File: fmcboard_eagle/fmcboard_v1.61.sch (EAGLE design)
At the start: 202 parts, among them IC1 OPA695IDR, IC10 LM358, IC11 7805TV, IC12 SN74AUC2G66DCTR, IC13 SN74AUC2G66DCTR, IC14 SN74AUC2G66DCTR, IC15 SN74AUC2G66DCTR, IC16 DAC7578SPWR, IC17 SN74AUC2G66DCTR, IC18 SN74AUC2G66DCTR, IC19 SN74AUC2G66DCTR, IC2 DAC7578SPWR, IC20 SN74AUC2G66DCTR, IC21 74AUP2GU04GW, IC22 74AUP2GU04GW, IC23 74AUP2GU04GW, IC24 74AUP2GU04GW, IC26 AMS1117-1.8, IC27 OPA699ID, IC3 LTC6229IMS8E#TRPBF, IC4 OPA695IDR, IC5 LTC6229IMS8E#TRPBF, IC6 OPA695IDR, IC7 OPA699ID, IC8 LM358, IC9 LM358, J1 8pin, J12 4p-2.54, J2 ASP-134604-01, J3 4p-2.54, J4 4p-2.54, J5 8pin, J6 4p-2.54, J7 4p-2.54, J8 4p-2.54, J9 8pin, U1 TXS0108EPWR, U2 STMICROELECTRONICS_L7905ACVST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

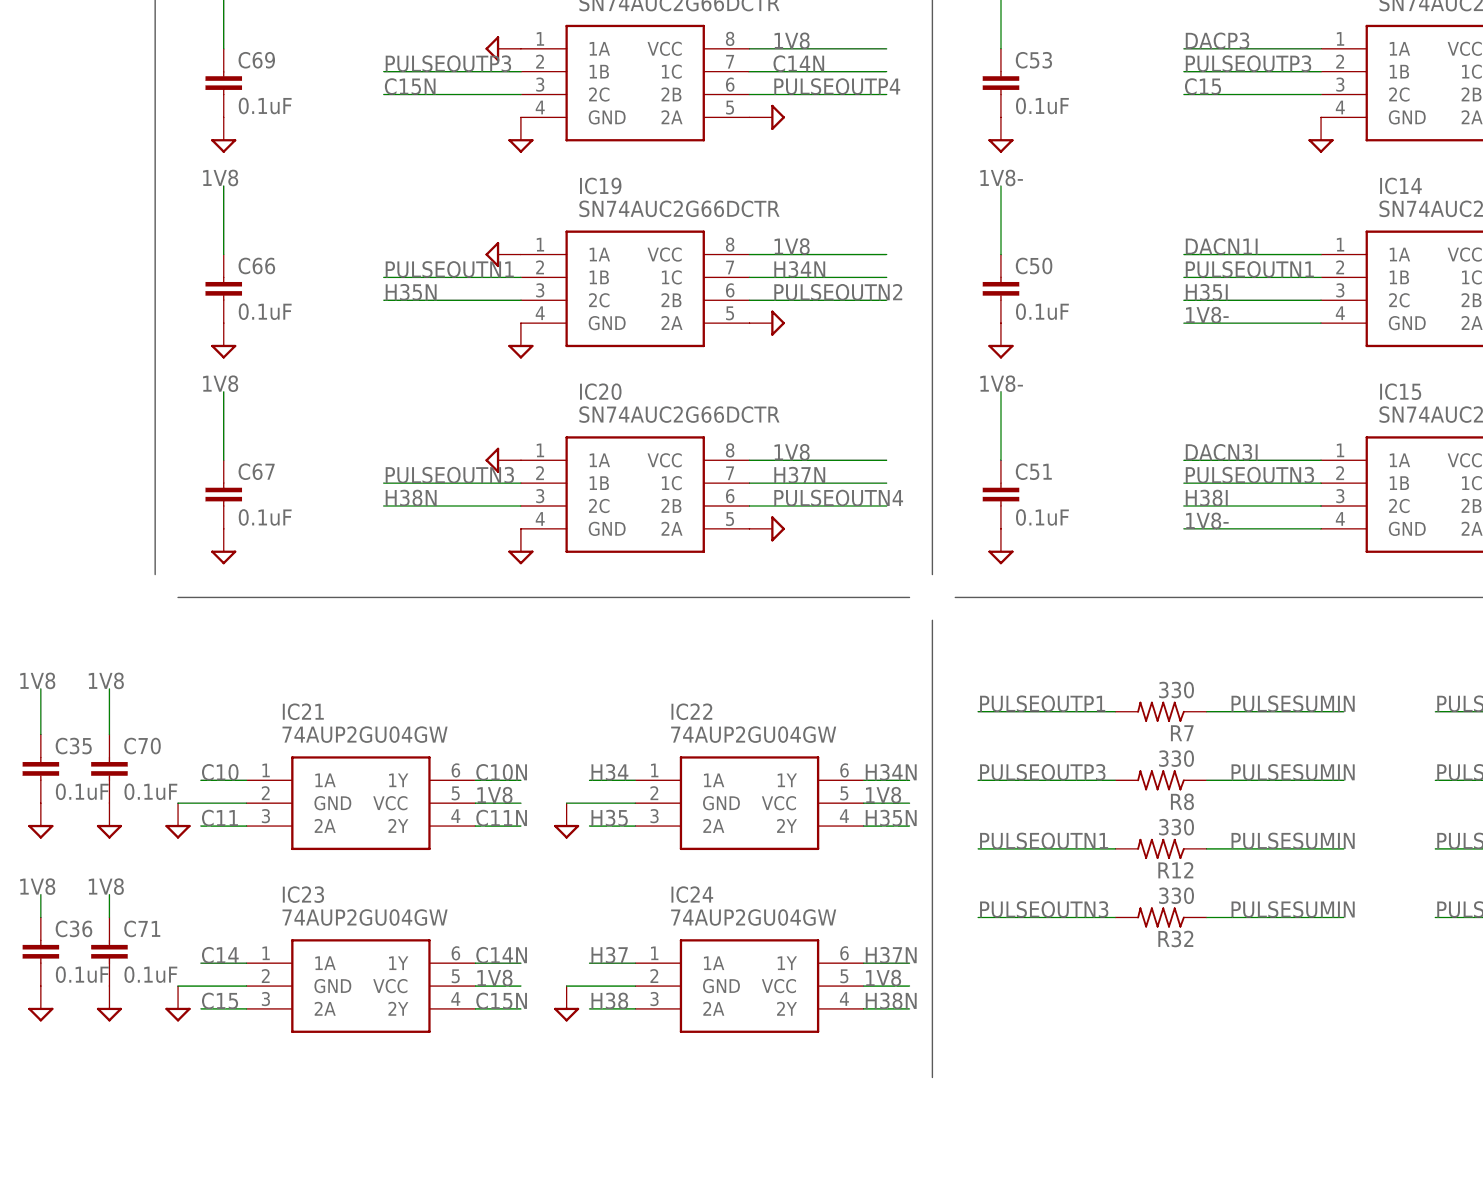
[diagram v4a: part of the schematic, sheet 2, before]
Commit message: use 1.8- and gnd for negative switches to gnd add 100 ohm resistors to inverting opa695s
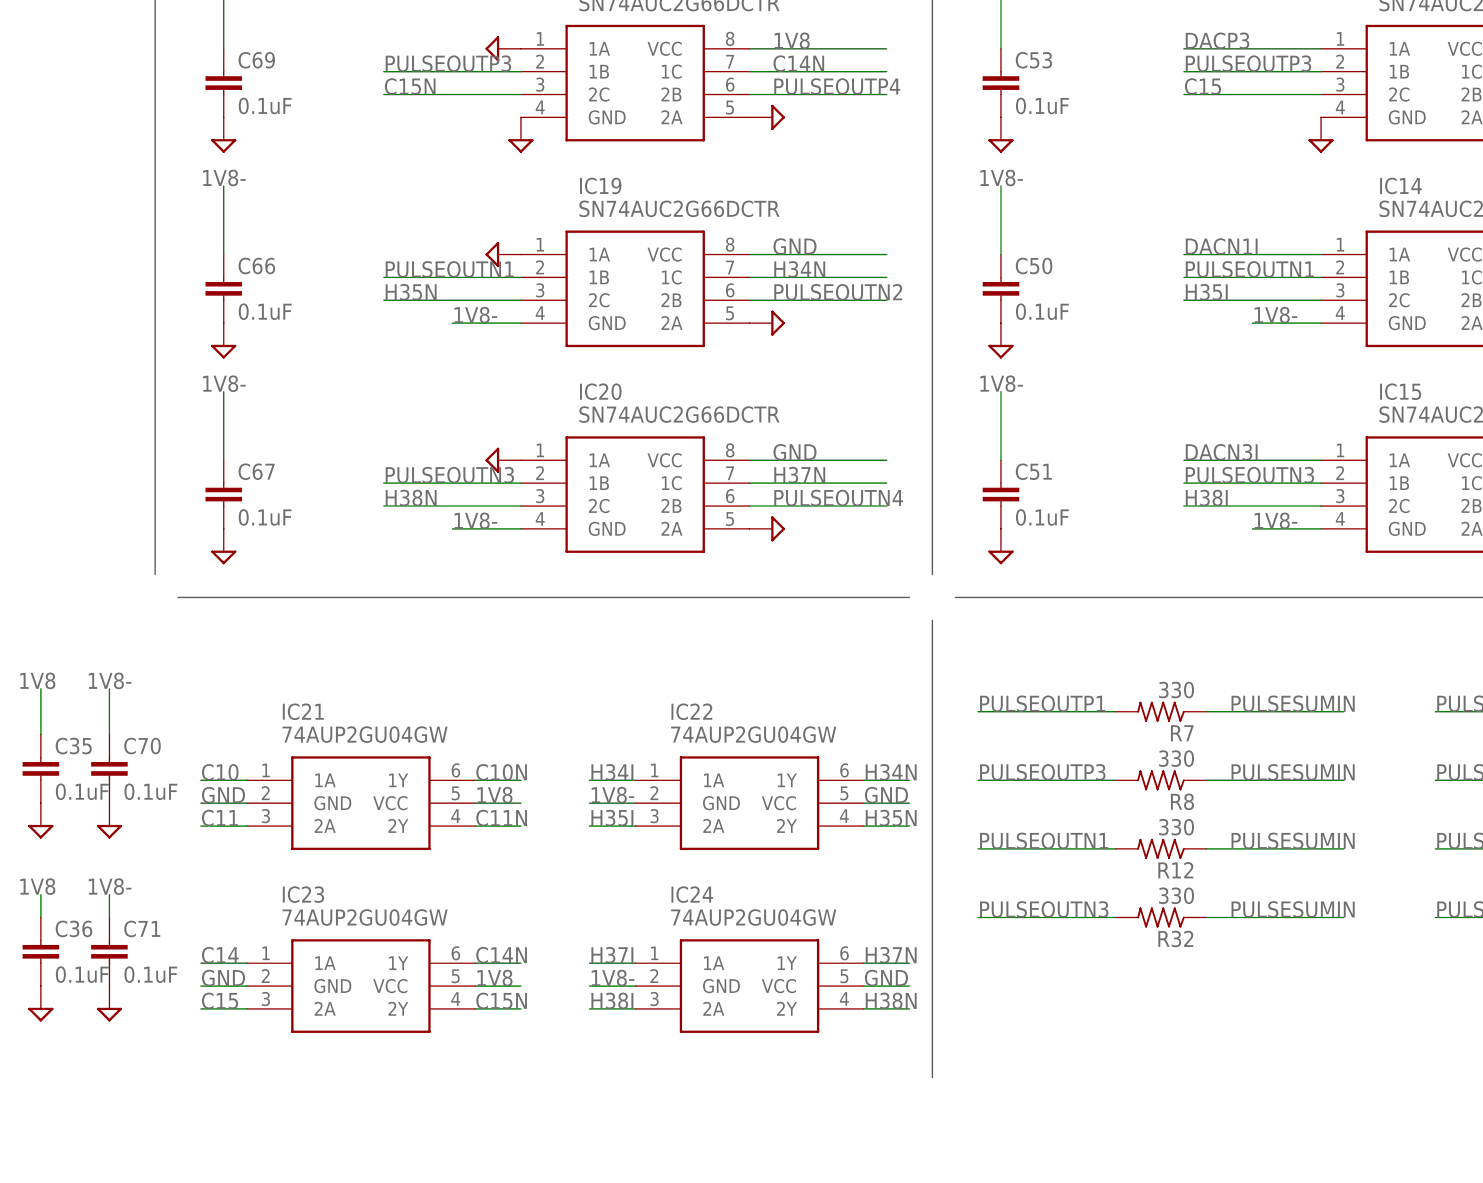
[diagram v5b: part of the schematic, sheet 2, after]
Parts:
- added R13, R3: 100, rcl:R-US_R0805
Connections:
- removed net H10: J2.H10, SV1.4
- removed net OP2BUF: IC27.NONINVERTING_INPUT, IC7.OUTPUT, R6.2
- new net N$3: IC1.NONINVERTING_INPUT, R3.1
- new net N$8: IC4.NONINVERTING_INPUT, R13.1
- new net OPOUT_H10: IC27.NONINVERTING_INPUT, IC7.OUTPUT, J2.H10, R6.2, SV1.4
- net 1V8: no longer C66.1, C67.1, C70.1, C71.1, IC19.VCC, IC20.VCC, IC22.VCC, IC24.VCC
- net 1V8-: now also C66.1, C67.1, C70.1, C71.1, IC19.GND, IC20.GND, IC22.GND, IC24.GND
- net GND: now also IC19.VCC, IC20.VCC, IC22.VCC, IC24.VCC, R13.2, R3.2; no longer IC1.NONINVERTING_INPUT, IC19.GND, IC20.GND, IC22.GND, IC24.GND, IC4.NONINVERTING_INPUT
- net H34: no longer IC22.1A
- net H34I: now also IC22.1A
- net H35: no longer IC22.2A
- net H35I: now also IC22.2A
- net H37: no longer IC24.1A
- net H37I: now also IC24.1A
- net H38: no longer IC24.2A
- net H38I: now also IC24.2A

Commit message: add dac pulse offsets + and -
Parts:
- added C11, C80: 1uF, SparkFun-Passives:CAP0805
- added C33, C65: 0.1uF, SparkFun-Passives:CAP0805
- added IC25: LM358, SparkFun-IC-Amplifiers:OPAMP-DUALU
- added R14, R35, R61, R70, R79, R85: 1k, rcl:R-US_R0805
- added R73, R84: 100, rcl:R-US_R0805
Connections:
- new net N$30: IC25G2.OUT, R14.2
- new net N$36: IC25G1.OUT, R35.2, R73.2
- new net N$37: IC25G1.-IN, R35.1, R61.1
- new net N$38: IC25G2.-IN, R14.1, R70.1
- new net N$39: IC16.VOUTB, R84.2
- new net PULSEOFFSET_N: IC16.VOUTD, R61.2
- new net PULSEOFFSET_NI: C11.2, R73.1, R85.2
- new net PULSEOFFSET_P: C80.1, R79.2, R84.1
- net GND: now also C11.1, C33.2, C65.2, C80.2, IC25G1.+IN, IC25G2.+IN, R70.2
- net PULSESUMIN: now also R79.1, R85.1
- net VS+: now also C33.1, IC25G3.P$V+
- net VS-: now also C65.1, IC25G3.P$V-
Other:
- note added: "Neg DAC offsets"
- note added: "Unused"
- moved on the sheet: C35, C36, C4, C70, C71, IC1, IC10G2, IC16, IC2, IC21, IC22, IC23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
